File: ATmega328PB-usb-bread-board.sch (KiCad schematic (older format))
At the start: 27 parts, among them J1 Conn_01x17, J2 Conn_01x17, J3 USB_B_Micro, J4 AVR-ISP-6, J5 Grove-I2C-connector, J6 Grove-I2C-connector, J7 Grove-I2C-connector, U1 ATmega328PB-MU, U2 CP2102N-A01-GQFN28, U5 SiT2001B-MEMS-Clock-Generator

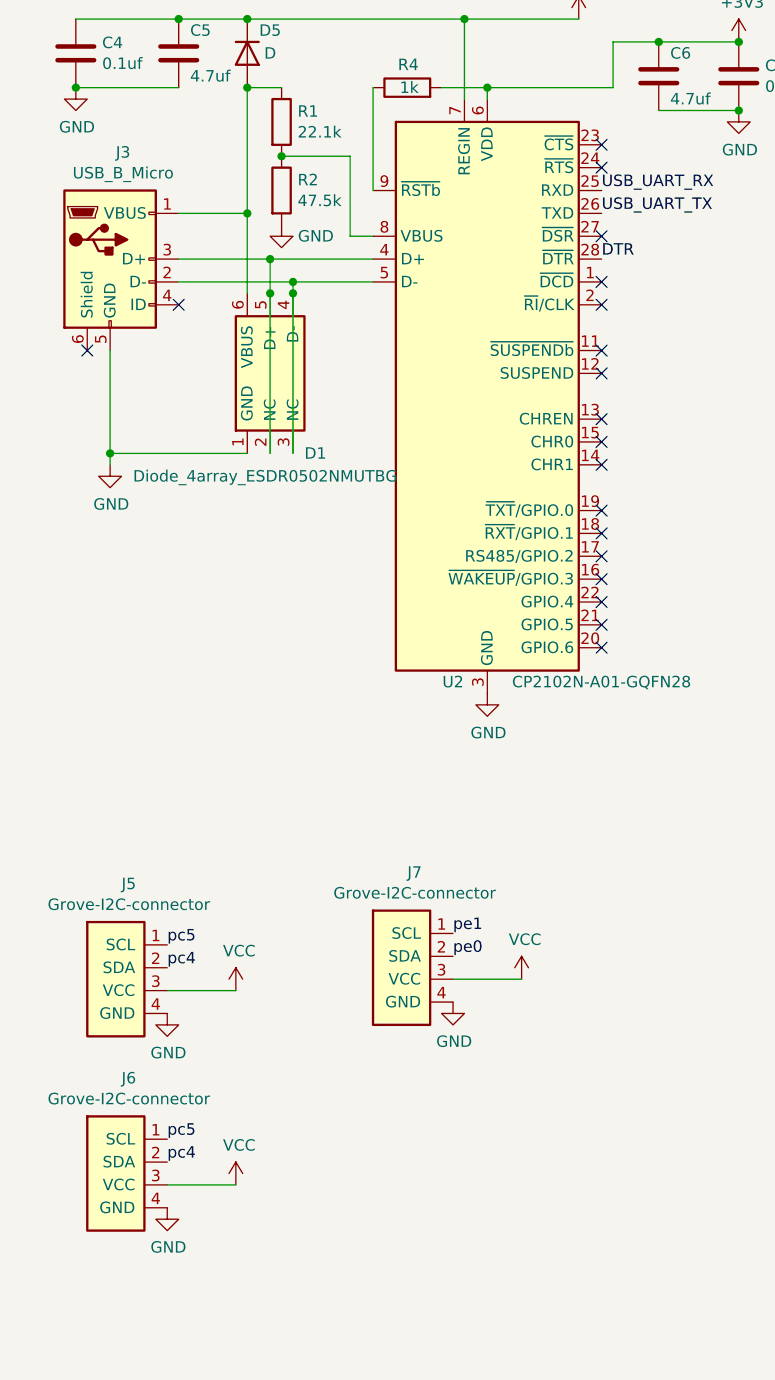
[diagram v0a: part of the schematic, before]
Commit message: Add USB pads
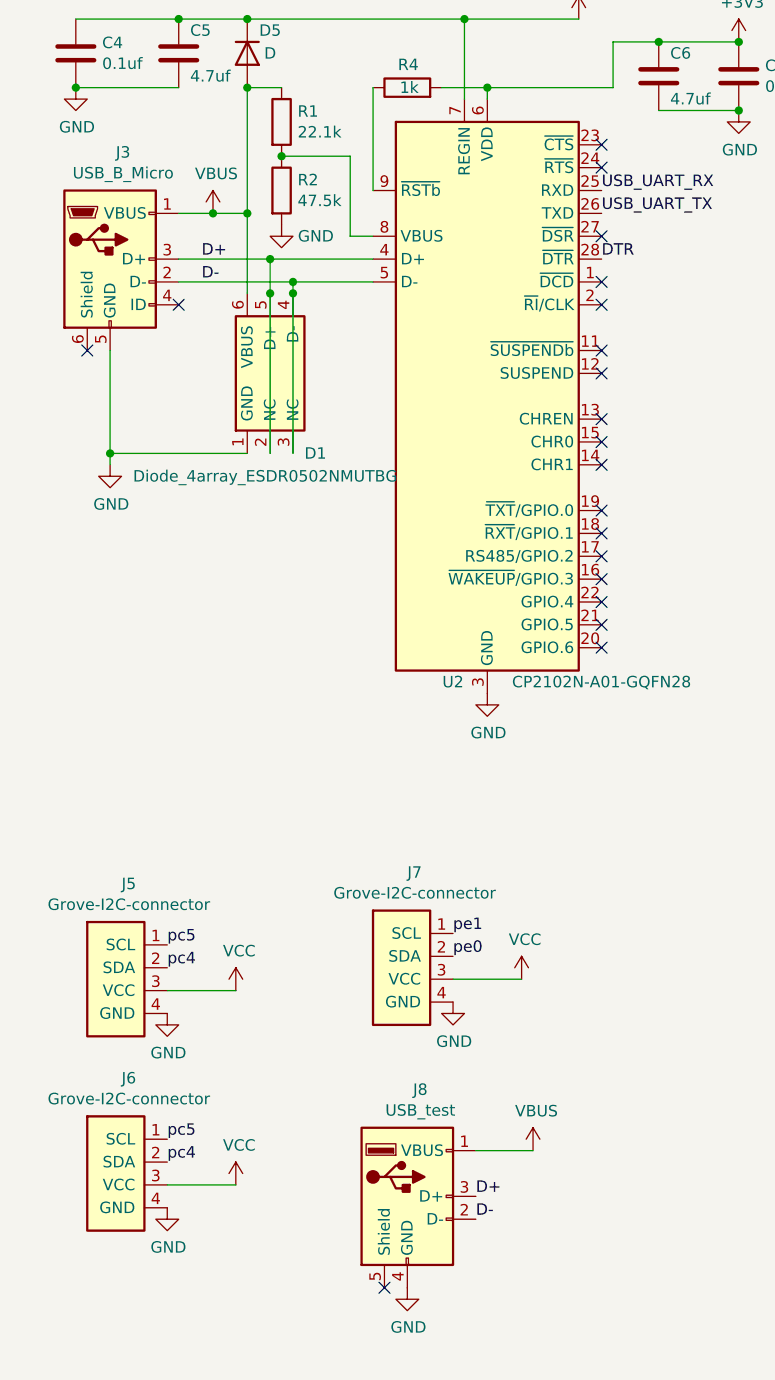
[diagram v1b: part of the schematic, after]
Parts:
- added J8: USB_test, my-kicad-footprints:2x02_P2.54mm_USB_Pads, symbol Connector:USB_A
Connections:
- net GND: now also J8.4 (GND)
- net D+: now reaches D1.2 (NC), D1.5 (D+), J3.3 (D+), U2.4 (D+)
- net D+: now also J8.3 (D+)
- net D-: now reaches D1.3 (NC), D1.4 (D-), J3.2 (D-), U2.5 (D-)
- net D-: now also J8.2 (D-)
- net VBUS: now reaches D1.6 (VBUS), D5.2 (A), J3.1 (VBUS), R1.1
- net VBUS: now also J8.1 (VBUS)
- no-connect marks 20 -> 21
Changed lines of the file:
@@
 $EndComp
 Wire Wire Line
-	1900 2250 1600 2250
+	1900 2250 1750 2250
 Wire Wire Line
 	2350 2350 2450 2350
@@
 $EndComp
 $Comp
-L power:+3V3 #PWR?
+L power:+3V3 #PWR0120
 U 1 1 60A1FEB1
 P 9400 2950
-F 0 "#PWR?" H 9400 2800 50  0001 C CNN
+F 0 "#PWR0120" H 9400 2800 50  0001 C CNN
 F 1 "+3V3" H 9415 3123 50  0000 C CNN
 F 2 "" H 9400 2950 50  0001 C CNN
@@
 $EndComp
 Connection ~ 9400 2950
+$Comp
+L power:VBUS #PWR0121
+U 1 1 60A40CE6
+P 1750 2250
+F 0 "#PWR0121" H 1750 2100 50  0001 C CNN
+F 1 "VBUS" H 1765 2423 50  0000 C CNN
+F 2 "" H 1750 2250 50  0001 C CNN
+F 3 "" H 1750 2250 50  0001 C CNN
+	1    1750 2250
+	1    0    0    -1
+$EndComp
+Connection ~ 1750 2250
+Wire Wire Line
+	1750 2250 1600 2250
+$Comp
+L power:VBUS #PWR0127
+U 1 1 60A411E5
+P 3150 6350
+F 0 "#PWR0127" H 3150 6200 50  0001 C CNN
+F 1 "VBUS" H 3165 6523 50  0000 C CNN
+F 2 "" H 3150 6350 50  0001 C CNN
+F 3 "" H 3150 6350 50  0001 C CNN
+	1    3150 6350
+	1    0    0    -1
+$EndComp
+Wire Wire Line
+	3150 6350 2900 6350
+$Comp
+L power:GND #PWR0131
+U 1 1 60A44E2D
+P 2600 6950
+F 0 "#PWR0131" H 2600 6700 50  0001 C CNN
+F 1 "GND" H 2605 6777 50  0000 C CNN
+F 2 "" H 2600 6950 50  0001 C CNN
+F 3 "" H 2600 6950 50  0001 C CNN
+	1    2600 6950
+	1    0    0    -1
+$EndComp
+Text Label 1700 2450 0    50   ~ 0
+D+
+Text Label 1700 2550 0    50   ~ 0
+D-
+Text Label 2900 6550 0    50   ~ 0
+D+
+Text Label 2900 6650 0    50   ~ 0
+D-
+$Comp
+L Connector:USB_A J8
+U 1 1 60A50A78
+P 2600 6550
+F 0 "J8" H 2657 7017 50  0000 C CNN
+F 1 "USB_test" H 2657 6926 50  0000 C CNN
+F 2 "my-kicad-footprints:2x02_P2.54mm_USB_Pads" H 2750 6500 50  0001 C CNN
+F 3 " ~" H 2750 6500 50  0001 C CNN
+	1    2600 6550
+	1    0    0    -1
+$EndComp
+NoConn ~ 2500 6950
 $EndSCHEMATC

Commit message: Add reset button
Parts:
- added SW1: SW_Push, my-kicad-footprints:SW_Push_TVAF06, symbol Switch:SW_Push
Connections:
- net GND: now also SW1.1
- net pc6: now also SW1.2
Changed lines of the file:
@@
 $EndComp
 NoConn ~ 2500 6950
+Text Label 6550 5800 0    50   ~ 0
+pc6
+$Comp
+L power:GND #PWR0132
+U 1 1 60B73BE3
+P 6150 5800
+F 0 "#PWR0132" H 6150 5550 50  0001 C CNN
+F 1 "GND" H 6155 5627 50  0000 C CNN
+F 2 "" H 6150 5800 50  0001 C CNN
+F 3 "" H 6150 5800 50  0001 C CNN
+	1    6150 5800
+	1    0    0    -1
+$EndComp
+$Comp
+L Switch:SW_Push SW1
+U 1 1 60B7FEFC
+P 6350 5800
+F 0 "SW1" H 6350 6085 50  0000 C CNN
+F 1 "SW_Push" H 6350 5994 50  0000 C CNN
+F 2 "my-kicad-footprints:SW_Push_TVAF06" H 6350 6000 50  0001 C CNN
+F 3 "~" H 6350 6000 50  0001 C CNN
+	1    6350 5800
+	1    0    0    -1
+$EndComp
 $EndSCHEMATC

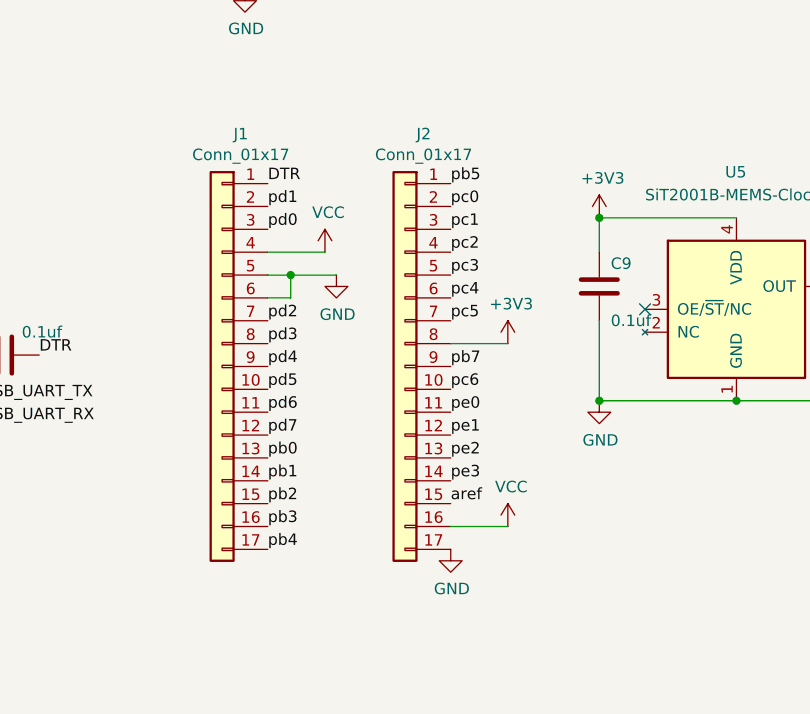
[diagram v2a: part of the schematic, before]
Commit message: Change position of D13
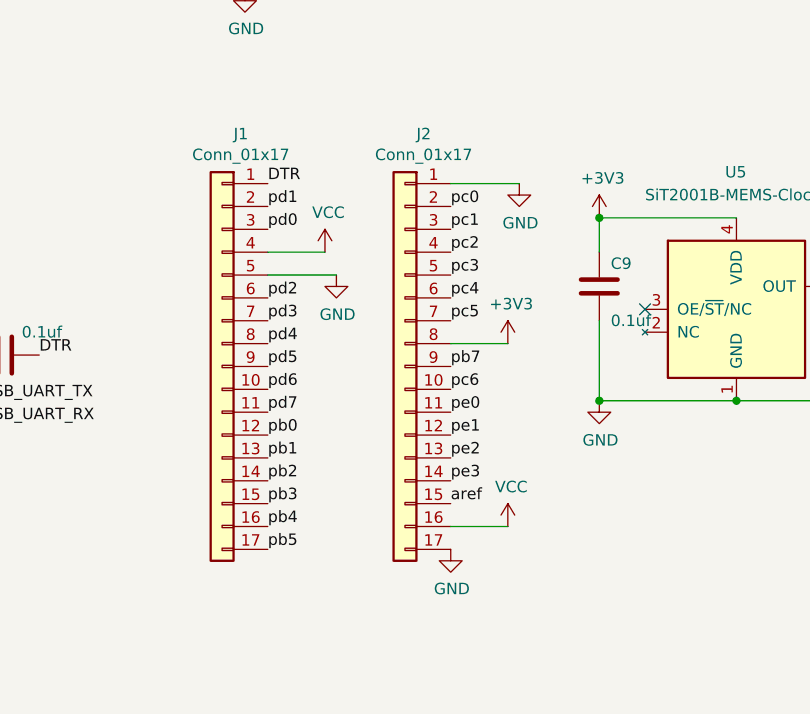
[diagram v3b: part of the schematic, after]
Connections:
- net GND: now also J2.1 (Pin_1); no longer J1.6 (Pin_6)
- net pb0: now also J1.12 (Pin_12); no longer J1.13 (Pin_13)
- net pb1: now also J1.13 (Pin_13); no longer J1.14 (Pin_14)
- net pb2: now also J1.14 (Pin_14); no longer J1.15 (Pin_15)
- net pb3: now also J1.15 (Pin_15); no longer J1.16 (Pin_16)
- net pb4: now also J1.16 (Pin_16); no longer J1.17 (Pin_17)
- net pb5: now also J1.17 (Pin_17); no longer J2.1 (Pin_1)
- net pd2: now also J1.6 (Pin_6); no longer J1.7 (Pin_7)
- net pd3: now also J1.7 (Pin_7); no longer J1.8 (Pin_8)
- net pd4: now also J1.8 (Pin_8); no longer J1.9 (Pin_9)
- net pd5: now also J1.9 (Pin_9); no longer J1.10 (Pin_10)
- net pd6: now also J1.10 (Pin_10); no longer J1.11 (Pin_11)
- net pd7: now also J1.11 (Pin_11); no longer J1.12 (Pin_12)
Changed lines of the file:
@@
 	1    0    0    -1
 $EndComp
-Text Label 8750 2800 0    50   ~ 0
+Text Label 7950 4400 0    50   ~ 0
 pb5
-Text Label 7950 4400 0    50   ~ 0
+Text Label 7950 4300 0    50   ~ 0
 pb4
-Text Label 7950 4300 0    50   ~ 0
+Text Label 7950 4200 0    50   ~ 0
 pb3
-Text Label 7950 4200 0    50   ~ 0
+Text Label 7950 4100 0    50   ~ 0
 pb2
-Text Label 7950 4100 0    50   ~ 0
+Text Label 7950 4000 0    50   ~ 0
 pb1
-Text Label 7950 4000 0    50   ~ 0
+Text Label 7950 3900 0    50   ~ 0
 pb0
-Text Label 7950 3900 0    50   ~ 0
+Text Label 7950 3800 0    50   ~ 0
 pd7
-Text Label 7950 3800 0    50   ~ 0
+Text Label 7950 3700 0    50   ~ 0
 pd6
-Text Label 7950 3700 0    50   ~ 0
+Text Label 7950 3600 0    50   ~ 0
 pd5
-Text Label 7950 3600 0    50   ~ 0
+Text Label 7950 3500 0    50   ~ 0
 pd4
-Text Label 7950 3500 0    50   ~ 0
+Text Label 7950 3400 0    50   ~ 0
 pd3
-Text Label 7950 3400 0    50   ~ 0
+Text Label 7950 3300 0    50   ~ 0
 pd2
 Text Label 8750 3000 0    50   ~ 0
@@
 Text Label 8750 3600 0    50   ~ 0
 pb7
-Wire Wire Line
-	8250 3200 8050 3200
 $Comp
 L power:VCC #PWR0108
@@
 	1    0    0    -1
 $EndComp
-Wire Wire Line
-	8050 3200 8050 3300
-Wire Wire Line
-	8050 3300 7950 3300
-Connection ~ 8050 3200
-Wire Wire Line
-	8050 3200 7950 3200
 $Comp
 L ATmega328PB-usb-bread-board-rescue:ATmega328PB-MU-MCU_Microchip_ATmega U1
@@
 	1    0    0    -1
 $EndComp
+Wire Wire Line
+	7950 3200 8250 3200
+$Comp
+L power:GND #PWR?
+U 1 1 60D27B13
+P 9050 2800
+F 0 "#PWR?" H 9050 2550 50  0001 C CNN
+F 1 "GND" H 9055 2627 50  0000 C CNN
+F 2 "" H 9050 2800 50  0001 C CNN
+F 3 "" H 9050 2800 50  0001 C CNN
+	1    9050 2800
+	1    0    0    -1
+$EndComp
+Wire Wire Line
+	9050 2800 8750 2800
 $EndSCHEMATC
